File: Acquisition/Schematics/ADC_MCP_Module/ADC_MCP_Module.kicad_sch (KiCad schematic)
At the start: 30 parts, among them J1 Can, J2 AudioJack4_SwitchTR1, J3 Conn_02x06_Counter_Clockwise, Q1 IRLML9301, SW1 SW_DIP_x01

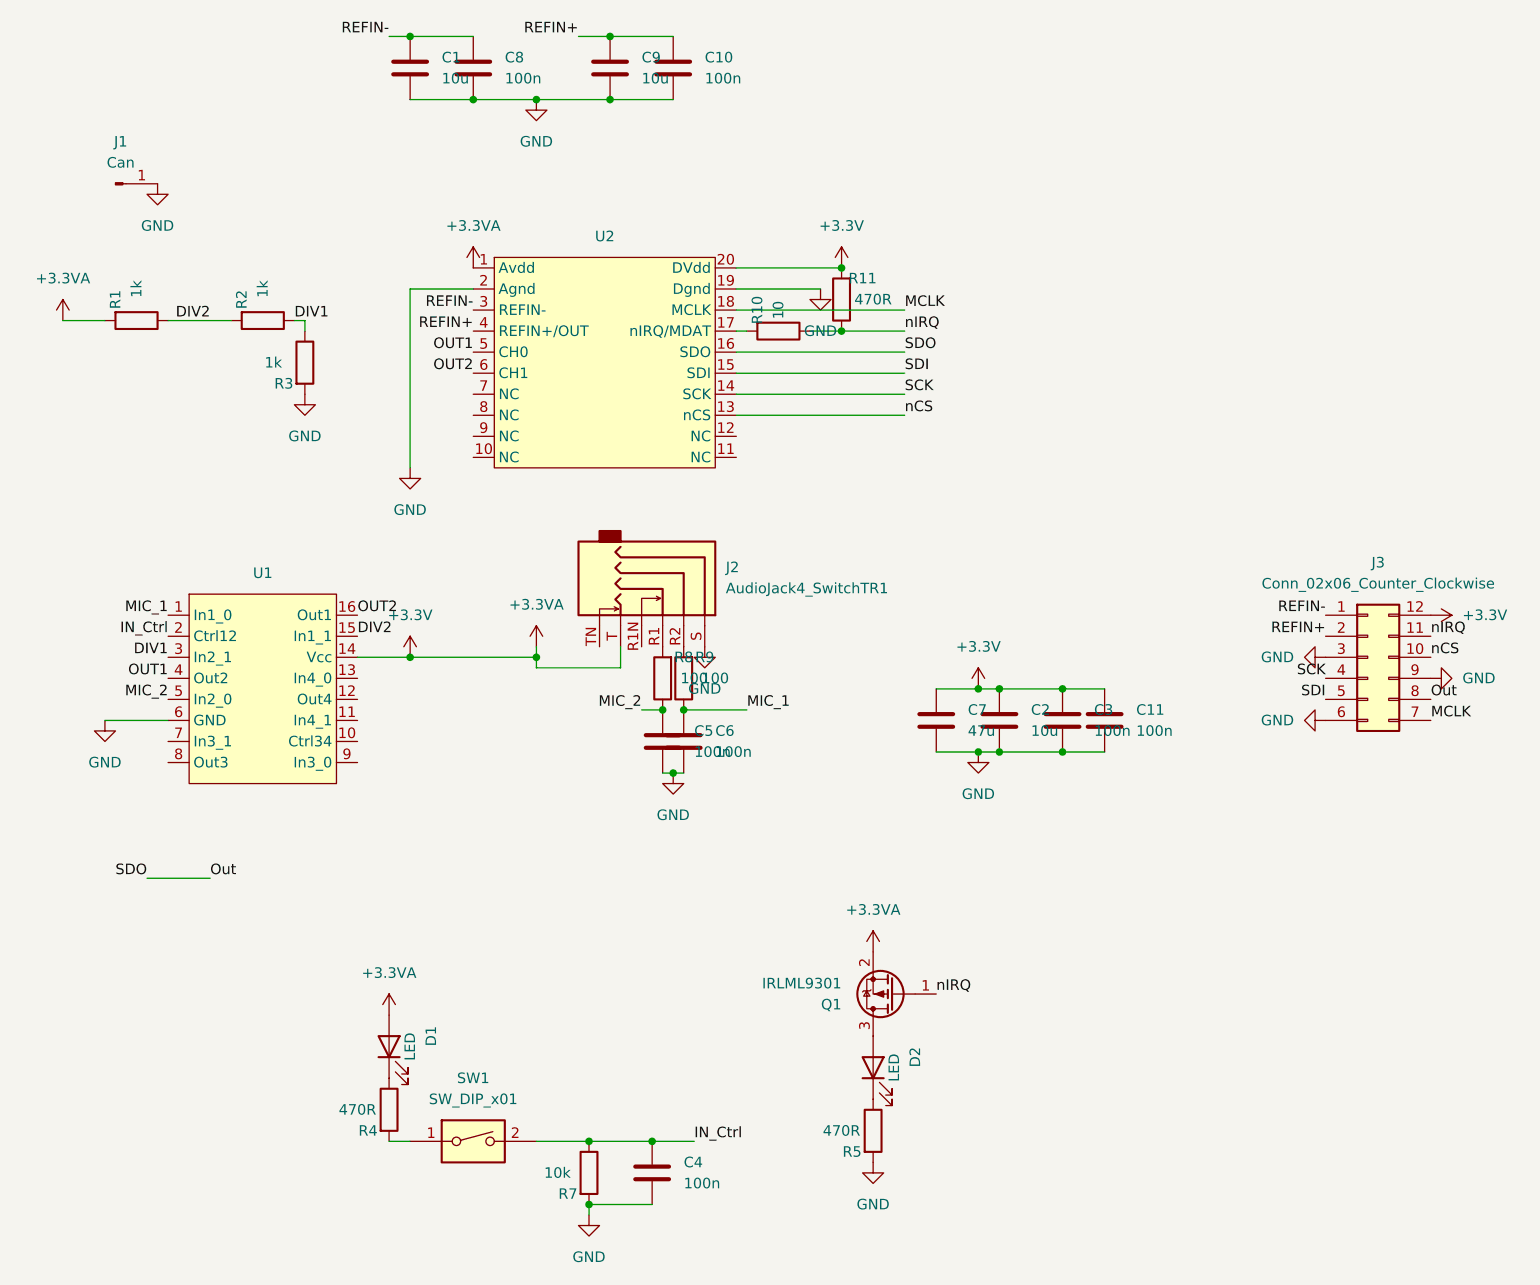
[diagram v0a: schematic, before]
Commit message: Schematics - FPGA board seems done
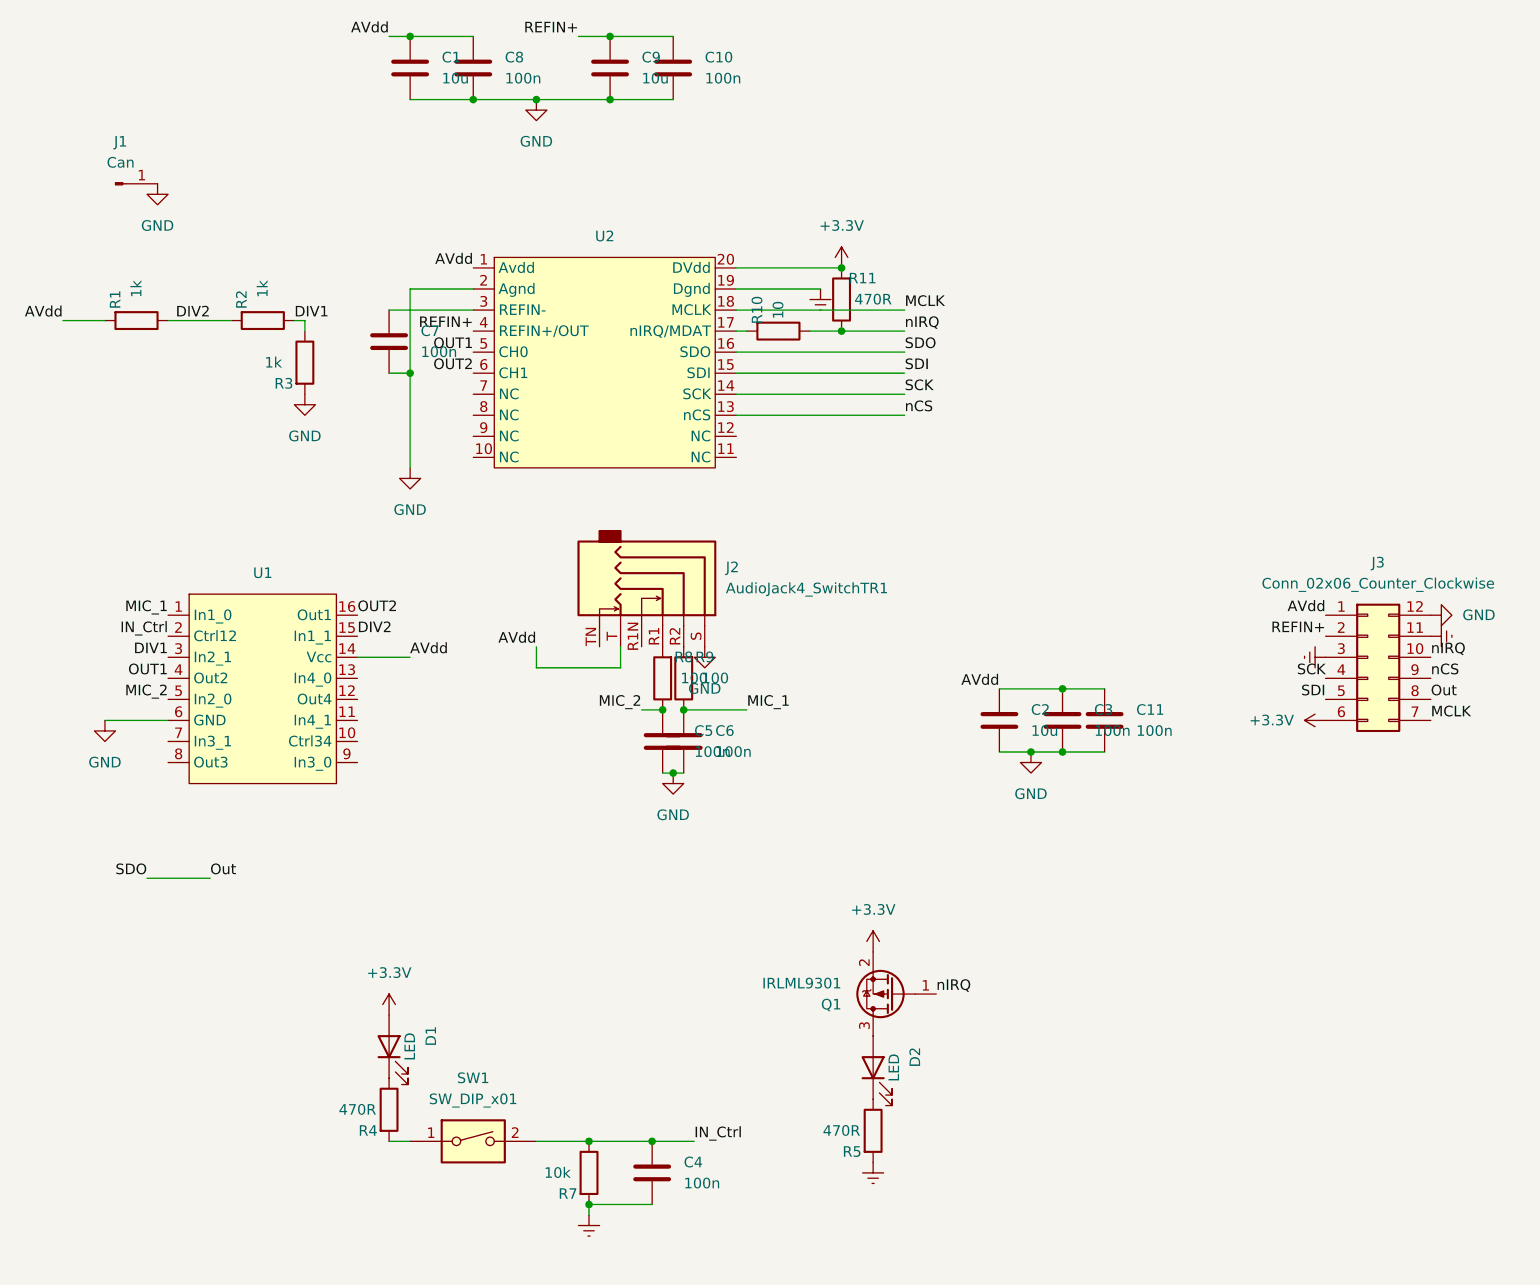
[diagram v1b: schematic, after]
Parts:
- C7: value 47u -> 100n; footprint Capacitor_Tantalum_SMD:CP_EIA-3528-21_Kemet-B -> Resistor_SMD:R_0402_1005Metric
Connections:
- net +3.3V: now also J3.6 (Pin_6); no longer C11.1, C2.1, C3.1, C7.1, J2.T, J3.12 (Pin_12), R1.2, U1.14 (Vcc), U2.1 (Avdd)
- net GND: now also J3.12 (Pin_12); no longer C4.2, J3.3 (Pin_3), J3.6 (Pin_6), J3.9 (Pin_9), R5.2, R7.2, U2.19 (Dgnd)
- net nCS: now also J3.9 (Pin_9); no longer J3.10 (Pin_10)
- net nIRQ: now also J3.10 (Pin_10); no longer J3.11 (Pin_11)
- net REFIN- renamed AVdd
- net AVdd: now also C11.1, C2.1, C3.1, J2.T, R1.2, U1.14 (Vcc), U2.1 (Avdd); no longer U2.3 (REFIN-)
- new net: C7.1, U2.3 (REFIN-)
- new net Earth: C4.2, J3.11 (Pin_11), J3.3 (Pin_3), R5.2, R7.2, U2.19 (Dgnd)

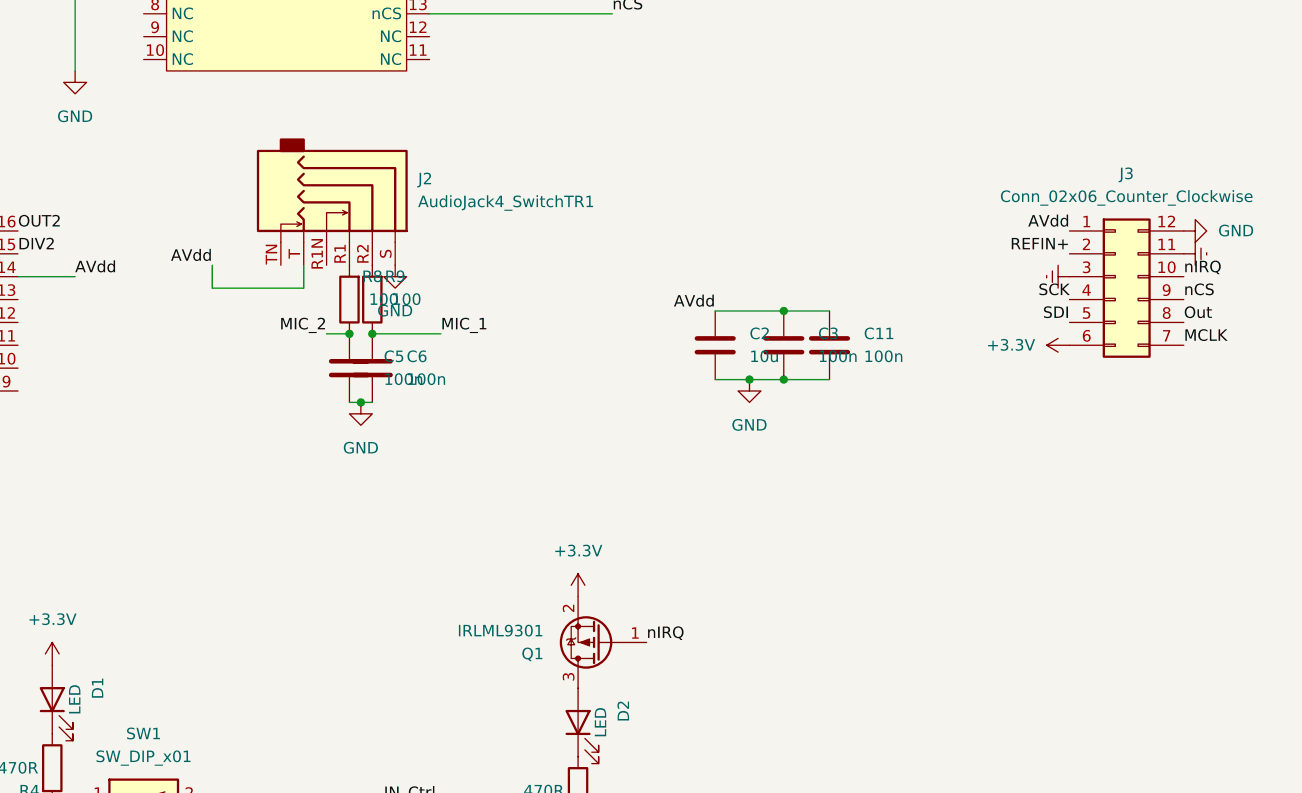
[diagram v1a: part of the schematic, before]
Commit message: Acquisition schematics should be working.
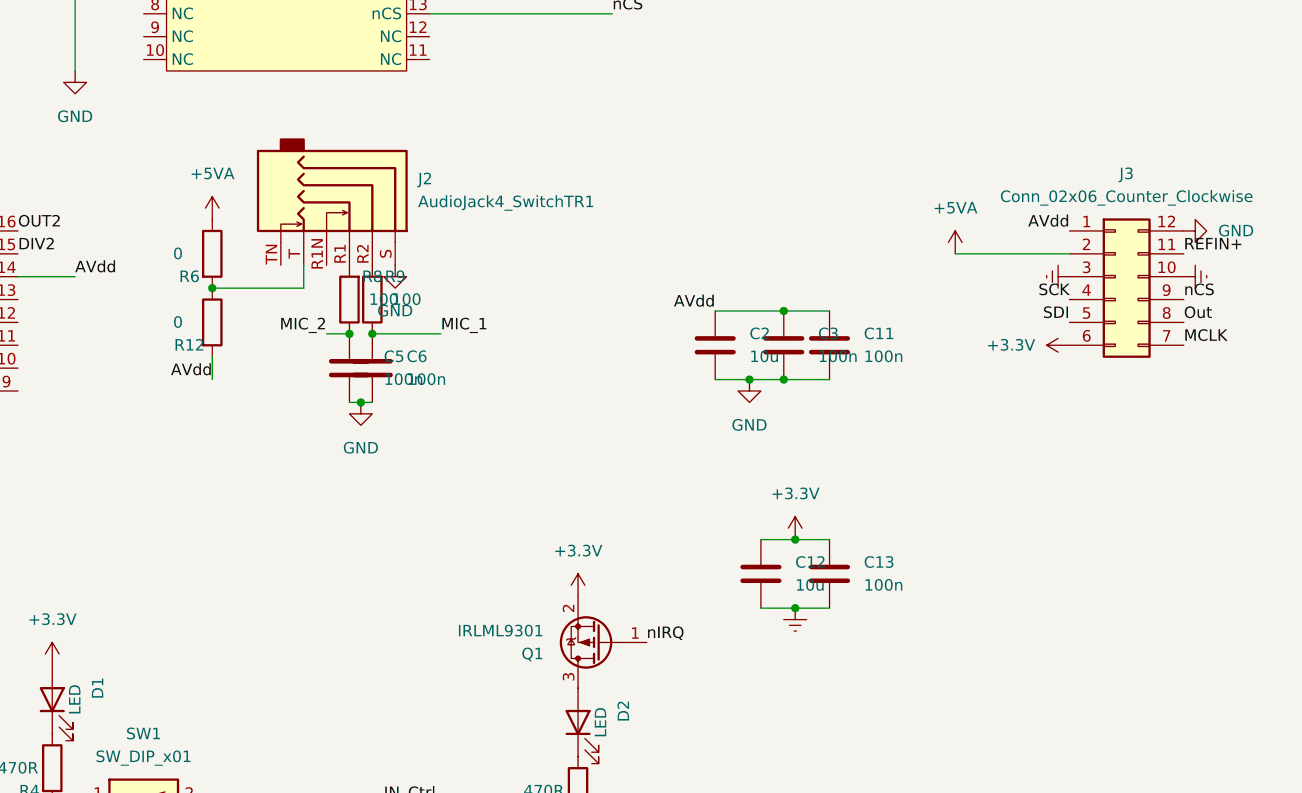
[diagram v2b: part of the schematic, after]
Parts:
- added C12: 10u, Resistor_SMD:R_0603_1608Metric, symbol Device:C
- added C13: 100n, Resistor_SMD:R_0402_1005Metric, symbol Device:C
- added R12, R6: 0, Resistor_SMD:R_0603_1608Metric, symbol Device:R
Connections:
- net +3.3V: now also C12.1, C13.1
- net AVdd: now also R12.2; no longer J2.T
- net Earth: now also J3.10 (Pin_10), C12.2, C13.2; no longer J3.11 (Pin_11)
- net REFIN+: now also J3.11 (Pin_11); no longer J3.2 (Pin_2)
- net nIRQ: no longer J3.10 (Pin_10)
- new net: J2.T, R12.1, R6.2
- new net +5VA: J3.2 (Pin_2), R6.1
